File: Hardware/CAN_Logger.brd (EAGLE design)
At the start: 48.3 x 20.8 mm, 56 parts, among them IC1 REG1117, Q1 8 MHz, U1 STM32F405XXSTM32F405XX, U4 MCP2551-E/SN, X2 22-23-2021, X4 22-23-2031, X5 MINI-USB-32005-301

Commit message: updated to hardware revision 2
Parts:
- removed C6: 0.1 u, rcl:C0603
- removed R1, R15: 22, resistor:R0603
- removed R16: 1 k, resistor:R0603
- removed R20: 4.7k, resistor:R0603
- removed U$2: MICROSD, adafruit:MICROSD
- removed X5: MINI-USB-32005-301, con-cypressindustries:32005-301
- added U$1: NONAME_SD, uSD:NONAME_SD
- C1: value 0.1 u -> 100 nF
- C10, C22: value 20p -> 18 pF
- C15, C21: value 2u2 -> 2.2 uF
- C16, C17, C19, C20, C23, C7: value 100 n -> 100 nF
- C2, C5: value 10u -> 10 uF x 25V
- C4: value 1u -> 2.2 uF
- C8, C9: value 560 -> 560 pF
- IC1: value REG1117 -> NCP1117ST33T3G
- LED1: value (none) -> Red
- LED2: value (none) -> Blue
- LED3: value (none) -> Green
- Q1: value 8 MHz -> ABLS2-8.000MHZ
- R11, R12: value 20 -> 22
- R13, R4: value 4.7k -> 4.7 k
- R14: value 22 -> 0; device resistor:R0603 -> rcl:R0402
- U1: value STM32F405XXSTM32F405XX -> STM32F405RGT6
- U4: value MCP2551-E/SN -> SN65HVD232DR
- moved X2 43.6 mm to (45.3, -2.10), turned to 90 degrees
- moved D2 41.1 mm to (40.4, -3.05), turned to 0 degrees
- moved C5 39.8 mm to (46.0, 4.00), turned to 270 degrees
- moved IC1 32.9 mm to (40.4, 3.94), turned to 90 degrees
- moved C4 23.7 mm to (35.6, 5.78), turned to 270 degrees
- moved R22 16.7 mm to (7.24, 12.9)
- moved R2 13.9 mm to (7.43, 11.5)
- moved C8 12.4 mm to (37.3, 8.06)
- moved R23 12.0 mm to (2.67, 13.8)
- moved C7 11.9 mm to (31.8, 11.3)
- moved R8 11.7 mm to (38.4, 14.5)
- moved R6 11.7 mm to (2.67, 12.1)
- moved U4 11.7 mm to (35.8, 11.3)
- moved X4 11.7 mm to (45.3, 11.2)
- moved R7 11.5 mm to (40.4, 8.06), turned to 180 degrees
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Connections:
- removed net N$3: R1.1, U$2.CD1
- removed net N$30: R16.2, U1.42
- removed net N$33: R15.2, X5.3
- removed net N$36: R14.2, X5.2
- removed net USB_VBUS: D2.1, R16.1, R20.1, X5.1
- new net N$2: D2.2, X2.2
- net +3V3: now also U$1.4; no longer U$2.4
- net GND: now also U$1.6, U$1.M1, U$1.M2, X2.1; no longer C6.2, R20.2, U$2.6, U$2.MT1, U$2.MT2, X2.2, X5.5
- net MMC_NCD: no longer R1.2
- net N$10: now also R14.1; no longer R9.2
- net N$11: now also U$1.2; no longer U$2.2
- net N$19: now also U$1.8; no longer U$2.8
- net N$20: now also U$1.1; no longer U$2.1
- net N$29: now also R14.2, R9.2; no longer D2.2, X2.1
- net N$4: now also U$1.3; no longer U$2.3
- net N$5: now also U$1.7; no longer U$2.7
- net N$6: now also U$1.5; no longer U$2.5
- net N$9: no longer C6.1
- net USB_DM: no longer R14.1
- net USB_DP: no longer R15.1
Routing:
- net USB_VBUS: track 47.1 -> 0.00 mm, vias 4 -> 0
- net +3V3: track 87.7 -> 124.0 mm, vias 7 -> 9
- net USB_DP: track 20.6 -> 0.00 mm
- net USB_DM: track 18.8 -> 0.00 mm
- net N$30: track 14.8 -> 0.00 mm, vias 2 -> 0
- net CAN2_RX: track 25.7 -> 12.8 mm
- net CAN2_TX: track 23.3 -> 12.2 mm
- net N$20: track 4.26 -> 14.5 mm, vias 1 -> 0
- net N$27: track 12.1 -> 22.1 mm
- net MMC_CLK: track 12.0 -> 2.90 mm
- net N$6: track 3.42 -> 11.5 mm, vias 1 -> 0
- net MMC_DAT0: track 24.5 -> 16.6 mm
- net MMC_DAT1: track 23.6 -> 15.7 mm
- net MMC_NCD: track 7.56 -> 0.00 mm
- net MMC_CMD: track 12.7 -> 5.28 mm
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
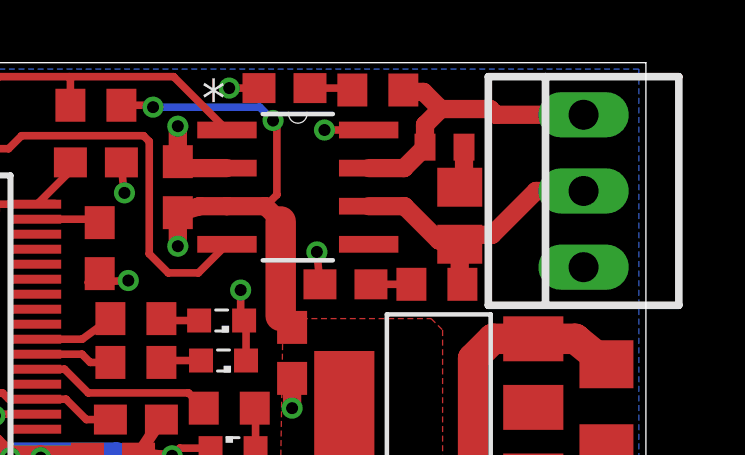
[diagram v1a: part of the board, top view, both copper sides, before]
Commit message: additional configuartion options for start/stop logs implemented
start_on_power, circular_write, start_id, stop_id, start_on_CAN, stop_on_CAN, start_frame_to_name
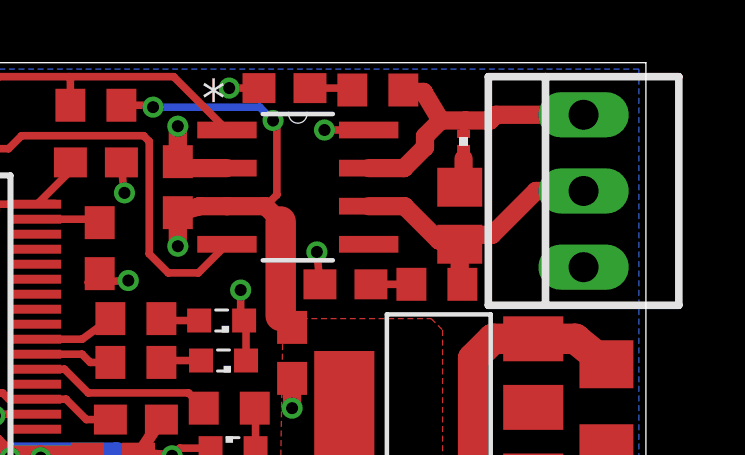
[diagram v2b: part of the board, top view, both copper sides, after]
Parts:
- R14: device rcl:R0402 -> rcl:R0201
- moved R14 0.66 mm to (41.3, 12.8), turned to 270 degrees
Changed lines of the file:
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@@
 <attribute name="VALUE" x="34.6075" y="-2.032" size="1.27" layer="27" rot="R180"/>
 </element>
-<element name="R14" library="rcl" package="R0402" value="0" x="40.64" y="12.6365" smashed="yes">
-<attribute name="VALUE" x="40.005" y="10.7315" size="1.27" layer="27"/>
+<element name="R14" library="rcl" package="R0201" value="0" x="41.275" y="12.827" smashed="yes" rot="R270">
+<attribute name="VALUE" x="39.37" y="13.462" size="1.27" layer="27" rot="R270"/>
 </element>
 <element name="U$1" library="uSD" package="NONAME_SD" value="NONAME_SD" x="11.557" y="10.795" smashed="yes" rot="R180">
@@
 <wire x1="39.331" y1="14.478" x2="39.2675" y2="14.5415" width="0.6096" layer="1"/>
 <wire x1="38.1127" y1="11.938" x2="39.2915" y2="11.938" width="0.6096" layer="1"/>
-<wire x1="39.2915" y1="11.938" x2="39.99" y2="12.6365" width="0.6096" layer="1"/>
-<wire x1="39.99" y1="12.6365" x2="39.99" y2="13.3835" width="0.6096" layer="1"/>
-<wire x1="39.99" y1="13.3835" x2="40.513" y2="13.9065" width="0.6096" layer="1"/>
 <wire x1="39.331" y1="14.478" x2="39.9415" y2="14.478" width="0.6096" layer="1"/>
-<wire x1="39.9415" y1="14.478" x2="40.513" y2="13.9065" width="0.6096" layer="1"/>
-<wire x1="42.164" y1="13.9065" x2="40.513" y2="13.9065" width="0.6096" layer="1"/>
+<wire x1="39.9415" y1="14.478" x2="40.513" y2="13.5255" width="0.6096" layer="1"/>
+<wire x1="42.164" y1="13.5255" x2="41.3385" y2="13.5255" width="0.6096" layer="1"/>
+<wire x1="41.3385" y1="13.5255" x2="40.513" y2="13.5255" width="0.6096" layer="1"/>
 <wire x1="45.2755" y1="13.716" x2="42.3545" y2="13.716" width="0.6096" layer="1"/>
-<wire x1="42.3545" y1="13.716" x2="42.164" y2="13.9065" width="0.6096" layer="1"/>
+<wire x1="42.3545" y1="13.716" x2="42.164" y2="13.5255" width="0.6096" layer="1"/>
+<wire x1="41.275" y1="13.082" x2="41.275" y2="13.3985" width="0.254" layer="1"/>
+<wire x1="39.99" y1="12.6365" x2="39.2915" y2="11.938" width="0.6096" layer="1"/>
+<wire x1="40.513" y1="13.5255" x2="39.99" y2="13.0025" width="0.6096" layer="1"/>
+<wire x1="39.99" y1="13.0025" x2="39.99" y2="12.6365" width="0.6096" layer="1"/>
+<wire x1="41.275" y1="13.3985" x2="41.275" y2="13.462" width="0.4064" layer="1"/>
+<wire x1="41.275" y1="13.462" x2="41.3385" y2="13.5255" width="0.4064" layer="1"/>
 </signal>
 <signal name="N$12">
@@
 <contactref element="R9" pad="2"/>
 <contactref element="R14" pad="2"/>
-<wire x1="41.29" y1="12.6365" x2="41.29" y2="11.4425" width="0.6096" layer="1"/>
 <wire x1="41.29" y1="11.4425" x2="41.148" y2="11.3005" width="0.6096" layer="1"/>
+<wire x1="41.275" y1="12.572" x2="41.275" y2="12.2555" width="0.254" layer="1"/>
+<wire x1="41.275" y1="12.2555" x2="41.275" y2="11.4275" width="0.6096" layer="1"/>
+<wire x1="41.275" y1="11.4275" x2="41.148" y2="11.3005" width="0.6096" layer="1"/>
 </signal>
 <signal name="N$20">
